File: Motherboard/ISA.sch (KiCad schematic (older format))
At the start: 2 parts, among them J2 Bus_ISA_8bit, J3 Bus_ISA_8bit

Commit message: A VERY large sync...
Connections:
- net GND: now reaches J2.1 (GND)
- net GND: now also J2.10 (GND), J2.31 (GND), J3.1 (GND), J3.10 (GND), J3.31 (GND)
- net +5V: now reaches J2.29 (VCC)
- net +5V: now also J2.3 (VCC), J3.29 (VCC), J3.3 (VCC)
- net -5V: now reaches J2.5 (-5V)
- net -5V: now also J3.5 (-5V)
- net -12V: now reaches J2.7 (-12V)
- net -12V: now also J3.7 (-12V)
- net +12V: now reaches J2.9 (+12V)
- net +12V: now also J3.9 (+12V)
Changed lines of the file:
@@
 $Descr A4 11693 8268
 encoding utf-8
-Sheet 5 5
+Sheet 5 8
 Title ""
 Date ""
@@
 	1    0    0    -1
 $EndComp
+$Comp
+L power:GND #PWR0110
+U 1 1 5C3285DE
+P 2275 1800
+F 0 "#PWR0110" H 2275 1550 50  0001 C CNN
+F 1 "GND" H 2280 1627 50  0000 C CNN
+F 2 "" H 2275 1800 50  0001 C CNN
+F 3 "" H 2275 1800 50  0001 C CNN
+	1    2275 1800
+	-1   0    0    1
+$EndComp
+Wire Wire Line
+	2275 1800 2275 1900
+Wire Wire Line
+	2275 1900 2350 1900
+$Comp
+L power:+5V #PWR0111
+U 1 1 5C3286C5
+P 2050 1800
+F 0 "#PWR0111" H 2050 1650 50  0001 C CNN
+F 1 "+5V" H 2065 1973 50  0000 C CNN
+F 2 "" H 2050 1800 50  0001 C CNN
+F 3 "" H 2050 1800 50  0001 C CNN
+	1    2050 1800
+	1    0    0    -1
+$EndComp
+Wire Wire Line
+	2050 1800 2050 2100
+Wire Wire Line
+	2050 2100 2350 2100
+$Comp
+L power:-5V #PWR0112
+U 1 1 5C3287A9
+P 2050 2300
+F 0 "#PWR0112" H 2050 2400 50  0001 C CNN
+F 1 "-5V" V 2065 2428 50  0000 L CNN
+F 2 "" H 2050 2300 50  0001 C CNN
+F 3 "" H 2050 2300 50  0001 C CNN
+	1    2050 2300
+	0    -1   -1   0
+$EndComp
+Wire Wire Line
+	2050 2300 2350 2300
+Wire Wire Line
+	2350 2500 2050 2500
+Wire Wire Line
+	2350 2700 2050 2700
+Wire Wire Line
+	2350 2800 2050 2800
+$Comp
+L power:-12V #PWR0113
+U 1 1 5C328963
+P 2050 2500
+F 0 "#PWR0113" H 2050 2600 50  0001 C CNN
+F 1 "-12V" V 2065 2628 50  0000 L CNN
+F 2 "" H 2050 2500 50  0001 C CNN
+F 3 "" H 2050 2500 50  0001 C CNN
+	1    2050 2500
+	0    -1   -1   0
+$EndComp
+$Comp
+L power:+12V #PWR0114
+U 1 1 5C3289C0
+P 2050 2700
+F 0 "#PWR0114" H 2050 2550 50  0001 C CNN
+F 1 "+12V" V 2065 2828 50  0000 L CNN
+F 2 "" H 2050 2700 50  0001 C CNN
+F 3 "" H 2050 2700 50  0001 C CNN
+	1    2050 2700
+	0    -1   -1   0
+$EndComp
+$Comp
+L power:GND #PWR0115
+U 1 1 5C328A08
+P 2050 2800
+F 0 "#PWR0115" H 2050 2550 50  0001 C CNN
+F 1 "GND" V 2055 2672 50  0000 R CNN
+F 2 "" H 2050 2800 50  0001 C CNN
+F 3 "" H 2050 2800 50  0001 C CNN
+	1    2050 2800
+	0    1    1    0
+$EndComp
+Wire Wire Line
+	2350 4700 2100 4700
+$Comp
+L power:+5V #PWR0116
+U 1 1 5C328B26
+P 2100 4700
+F 0 "#PWR0116" H 2100 4550 50  0001 C CNN
+F 1 "+5V" V 2115 4828 50  0000 L CNN
+F 2 "" H 2100 4700 50  0001 C CNN
+F 3 "" H 2100 4700 50  0001 C CNN
+	1    2100 4700
+	0    -1   -1   0
+$EndComp
+Wire Wire Line
+	2350 4900 2100 4900
+$Comp
+L power:GND #PWR0117
+U 1 1 5C328BFE
+P 2100 4900
+F 0 "#PWR0117" H 2100 4650 50  0001 C CNN
+F 1 "GND" V 2105 4772 50  0000 R CNN
+F 2 "" H 2100 4900 50  0001 C CNN
+F 3 "" H 2100 4900 50  0001 C CNN
+	1    2100 4900
+	0    1    1    0
+$EndComp
+$Comp
+L power:GND #PWR0118
+U 1 1 5C328D0A
+P 4850 1800
+F 0 "#PWR0118" H 4850 1550 50  0001 C CNN
+F 1 "GND" H 4855 1627 50  0000 C CNN
+F 2 "" H 4850 1800 50  0001 C CNN
+F 3 "" H 4850 1800 50  0001 C CNN
+	1    4850 1800
+	-1   0    0    1
+$EndComp
+Wire Wire Line
+	4850 1800 4850 1900
+Wire Wire Line
+	4850 1900 4925 1900
+$Comp
+L power:+5V #PWR0119
+U 1 1 5C328D12
+P 4625 1800
+F 0 "#PWR0119" H 4625 1650 50  0001 C CNN
+F 1 "+5V" H 4640 1973 50  0000 C CNN
+F 2 "" H 4625 1800 50  0001 C CNN
+F 3 "" H 4625 1800 50  0001 C CNN
+	1    4625 1800
+	1    0    0    -1
+$EndComp
+Wire Wire Line
+	4625 1800 4625 2100
+Wire Wire Line
+	4625 2100 4925 2100
+$Comp
+L power:-5V #PWR0120
+U 1 1 5C328D1A
+P 4625 2300
+F 0 "#PWR0120" H 4625 2400 50  0001 C CNN
+F 1 "-5V" V 4640 2428 50  0000 L CNN
+F 2 "" H 4625 2300 50  0001 C CNN
+F 3 "" H 4625 2300 50  0001 C CNN
+	1    4625 2300
+	0    -1   -1   0
+$EndComp
+Wire Wire Line
+	4625 2300 4925 2300
+Wire Wire Line
+	4925 2500 4625 2500
+Wire Wire Line
+	4925 2700 4625 2700
+Wire Wire Line
+	4925 2800 4625 2800
+$Comp
+L power:-12V #PWR0121
+U 1 1 5C328D24
+P 4625 2500
+F 0 "#PWR0121" H 4625 2600 50  0001 C CNN
+F 1 "-12V" V 4640 2628 50  0000 L CNN
+F 2 "" H 4625 2500 50  0001 C CNN
+F 3 "" H 4625 2500 50  0001 C CNN
+	1    4625 2500
+	0    -1   -1   0
+$EndComp
+$Comp
+L power:+12V #PWR0122
+U 1 1 5C328D2A
+P 4625 2700
+F 0 "#PWR0122" H 4625 2550 50  0001 C CNN
+F 1 "+12V" V 4640 2828 50  0000 L CNN
+F 2 "" H 4625 2700 50  0001 C CNN
+F 3 "" H 4625 2700 50  0001 C CNN
+	1    4625 2700
+	0    -1   -1   0
+$EndComp
+$Comp
+L power:GND #PWR0123
+U 1 1 5C328D30
+P 4625 2800
+F 0 "#PWR0123" H 4625 2550 50  0001 C CNN
+F 1 "GND" V 4630 2672 50  0000 R CNN
+F 2 "" H 4625 2800 50  0001 C CNN
+F 3 "" H 4625 2800 50  0001 C CNN
+	1    4625 2800
+	0    1    1    0
+$EndComp
+Wire Wire Line
+	4925 4700 4675 4700
+$Comp
+L power:+5V #PWR0124
+U 1 1 5C328D37
+P 4675 4700
+F 0 "#PWR0124" H 4675 4550 50  0001 C CNN
+F 1 "+5V" V 4690 4828 50  0000 L CNN
+F 2 "" H 4675 4700 50  0001 C CNN
+F 3 "" H 4675 4700 50  0001 C CNN
+	1    4675 4700
+	0    -1   -1   0
+$EndComp
+Wire Wire Line
+	4925 4900 4675 4900
+$Comp
+L power:GND #PWR0125
+U 1 1 5C328D3E
+P 4675 4900
+F 0 "#PWR0125" H 4675 4650 50  0001 C CNN
+F 1 "GND" V 4680 4772 50  0000 R CNN
+F 2 "" H 4675 4900 50  0001 C CNN
+F 3 "" H 4675 4900 50  0001 C CNN
+	1    4675 4900
+	0    1    1    0
+$EndComp
 $EndSCHEMATC

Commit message: Large sync
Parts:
- added J5, J6: Bus_ISA_8bit, RetPC:ISA-8-bit, symbol Connector:Bus_ISA_8bit
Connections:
- net +12V: now also J5.9 (+12V), J6.9 (+12V)
- net +5V: now also J5.29 (VCC), J5.3 (VCC), J6.29 (VCC), J6.3 (VCC)
- net -12V: now also J5.7 (-12V), J6.7 (-12V)
- net -5V: now also J5.5 (-5V), J6.5 (-5V)
- net GND: now also J5.1 (GND), J5.10 (GND), J5.31 (GND), J6.1 (GND), J6.10 (GND), J6.31 (GND)
- net RESET: now reaches J2.2 (RESET)
- net RESET: now also J3.2 (RESET), J5.2 (RESET), J6.2 (RESET)
- no-connect marks 0 -> 4

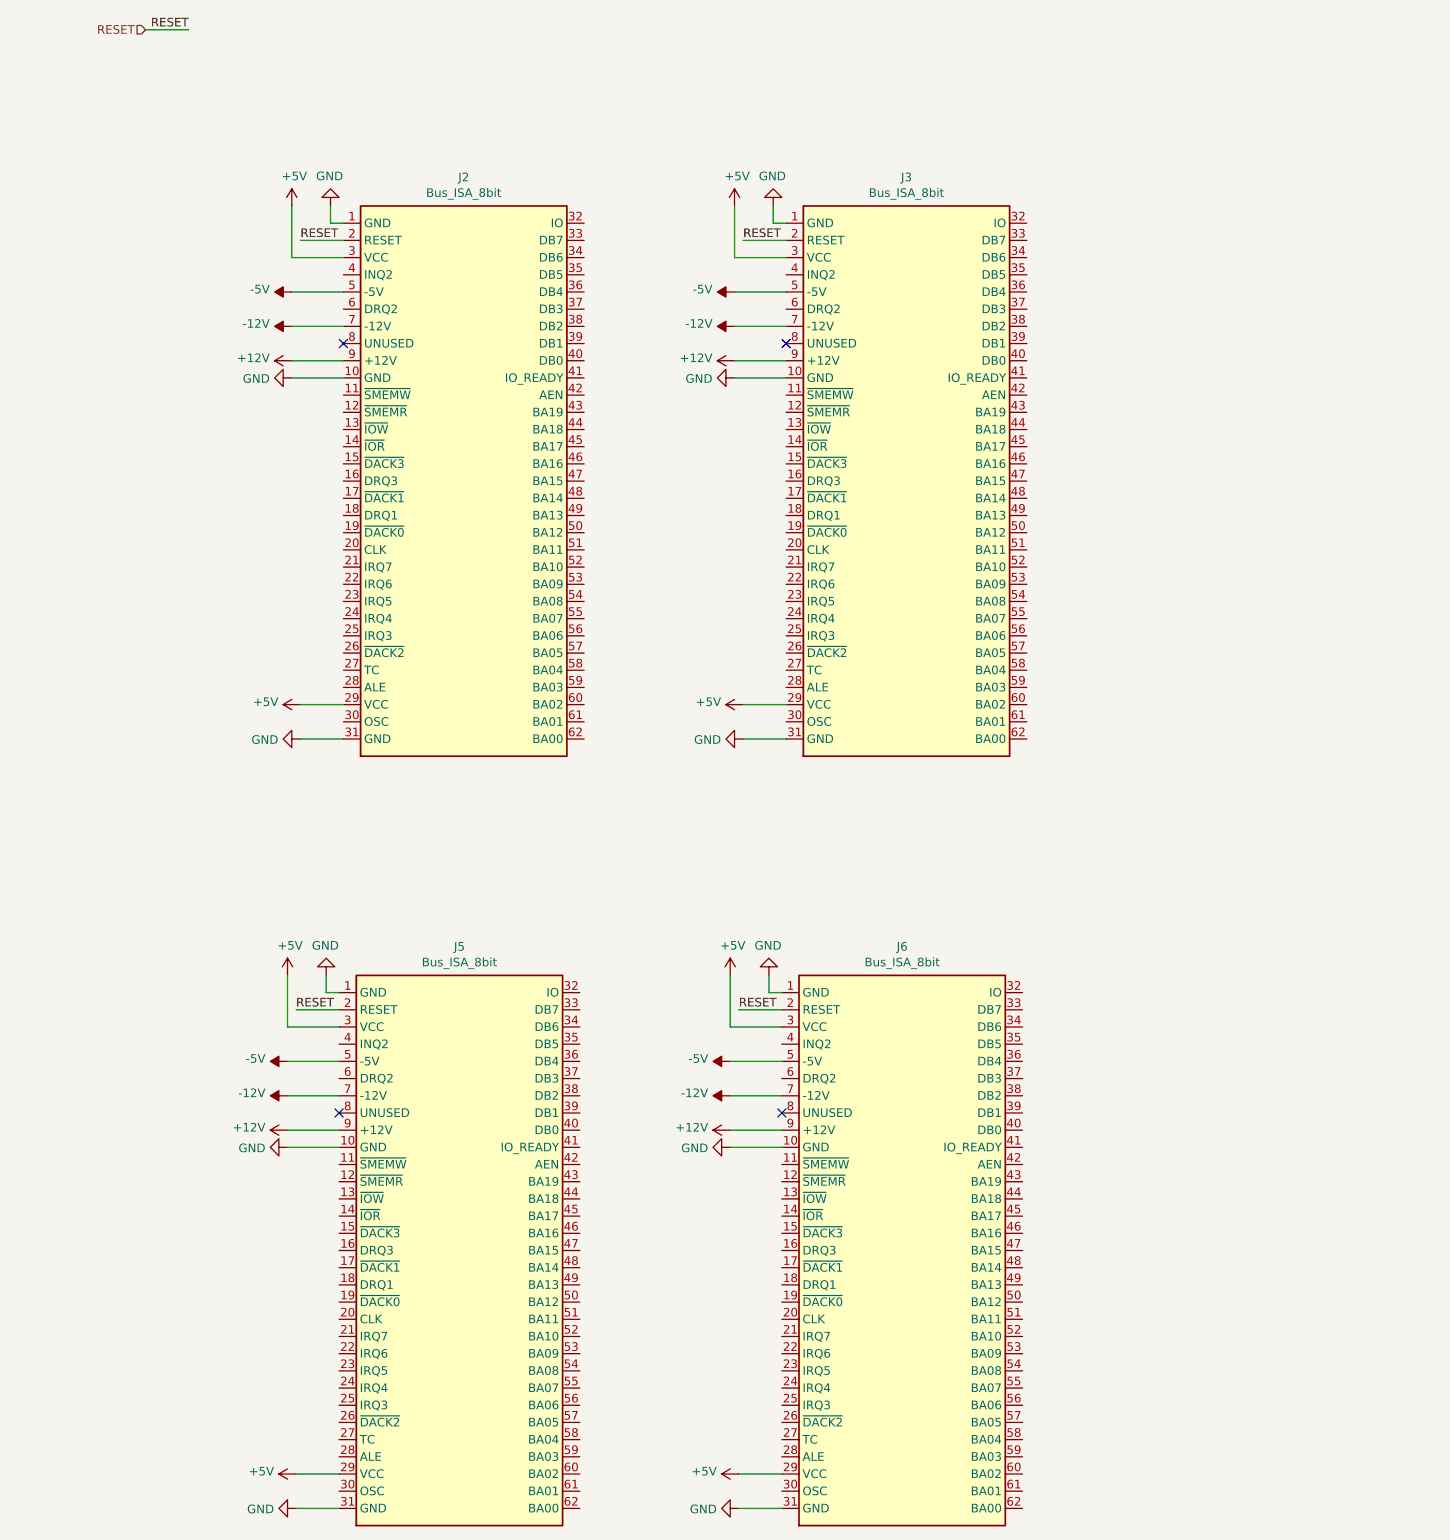
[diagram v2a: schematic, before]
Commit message: Work on motherboard  - Integrating glue logic into CPLD  - Began work on routing
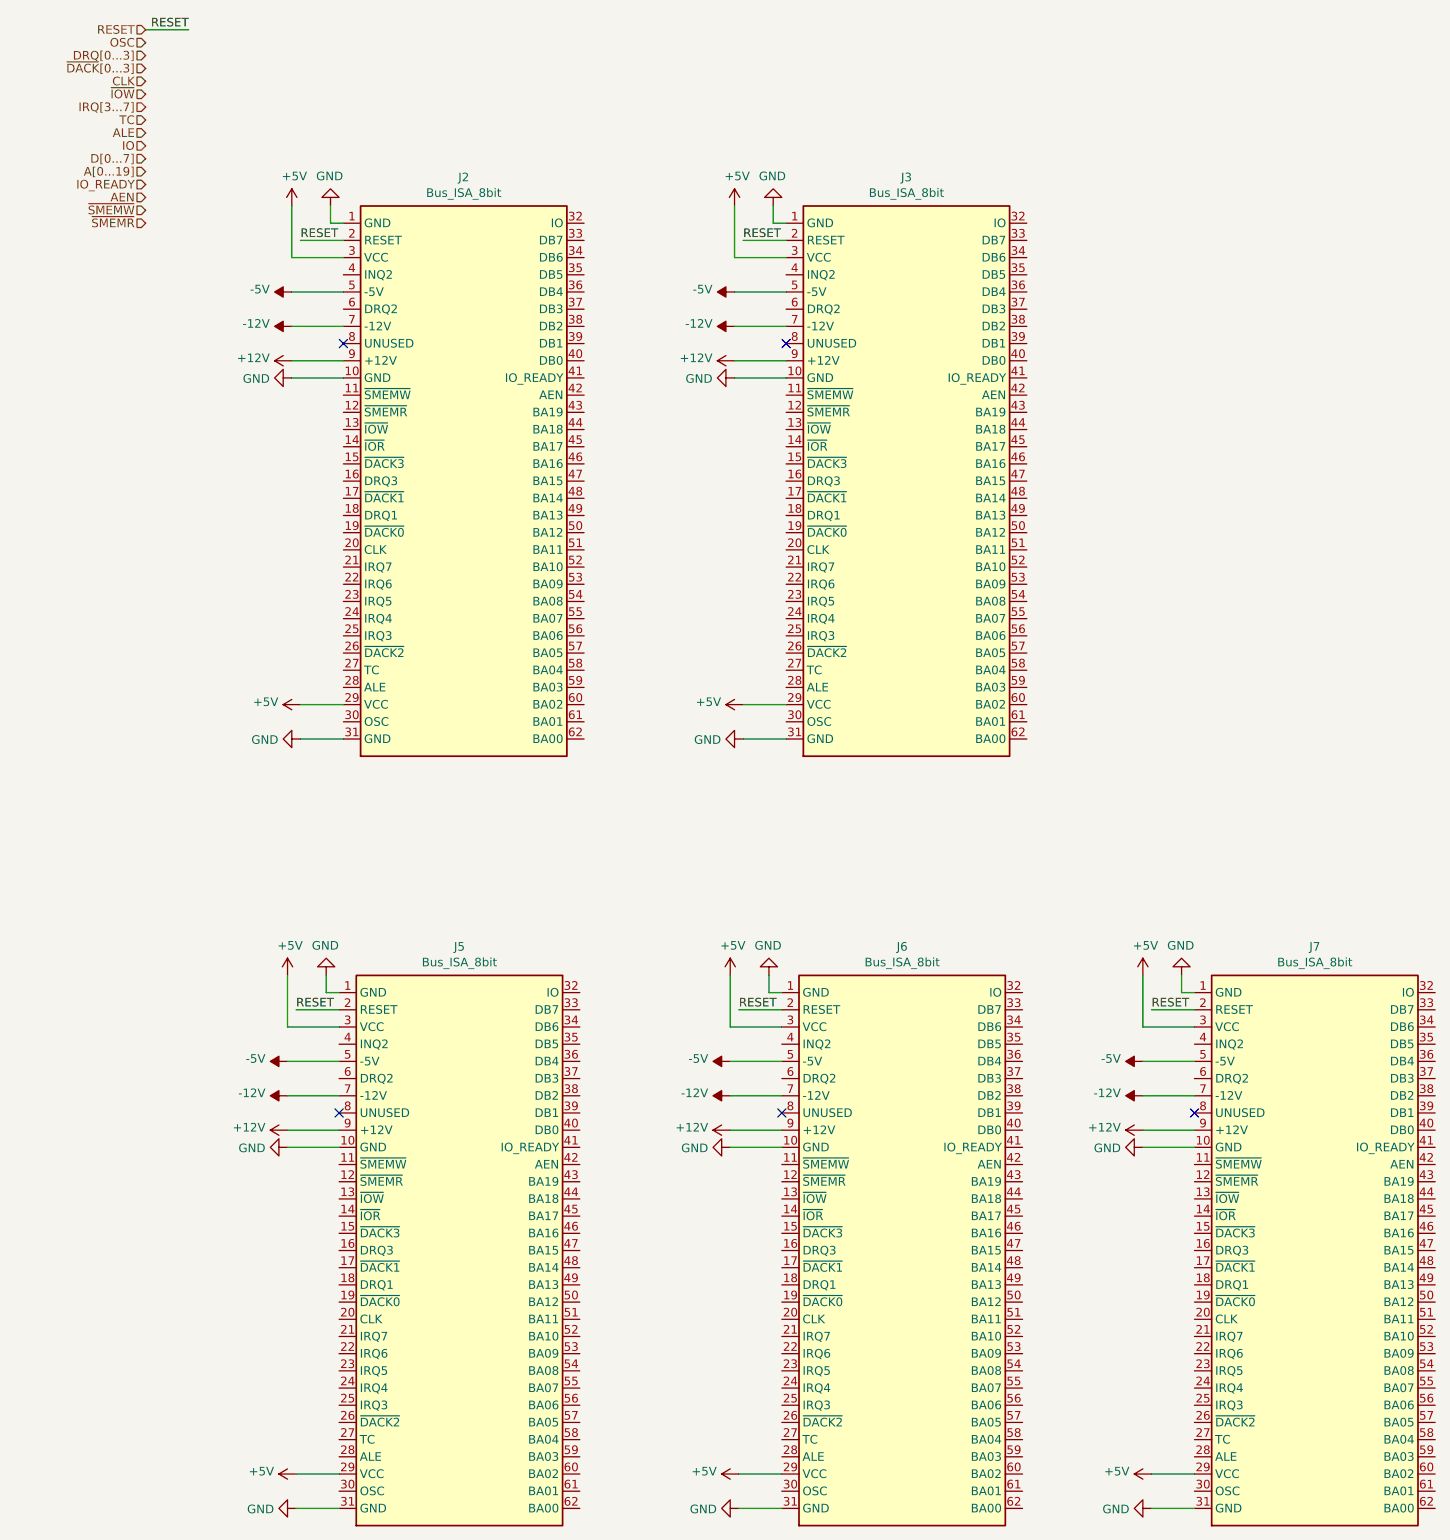
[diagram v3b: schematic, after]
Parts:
- added J7: Bus_ISA_8bit, RetPC:ISA-8-bit, symbol Connector:Bus_ISA_8bit
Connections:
- net +12V: now also J7.9 (+12V)
- net +5V: now also J7.29 (VCC), J7.3 (VCC)
- net -12V: now also J7.7 (-12V)
- net -5V: now also J7.5 (-5V)
- net GND: now also J7.1 (GND), J7.10 (GND), J7.31 (GND)
- net RESET: now also J7.2 (RESET)
- no-connect marks 4 -> 5
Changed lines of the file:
@@
 Text Label 4650 6475 0    50   ~ 0
 RESET
+$Comp
+L Connector:Bus_ISA_8bit J7
+U 1 1 5C5AC837
+P 8000 7875
+F 0 "J7" H 8000 9642 50  0000 C CNN
+F 1 "Bus_ISA_8bit" H 8000 9551 50  0000 C CNN
+F 2 "RetPC:ISA-8-bit" H 8000 7875 50  0001 C CNN
+F 3 "https://en.wikipedia.org/wiki/Industry_Standard_Architecture" H 8000 7875 50  0001 C CNN
+	1    8000 7875
+	1    0    0    -1
+$EndComp
+$Comp
+L power:GND #PWR0148
+U 1 1 5C5AC83D
+P 7225 6275
+F 0 "#PWR0148" H 7225 6025 50  0001 C CNN
+F 1 "GND" H 7230 6102 50  0000 C CNN
+F 2 "" H 7225 6275 50  0001 C CNN
+F 3 "" H 7225 6275 50  0001 C CNN
+	1    7225 6275
+	-1   0    0    1
+$EndComp
+Wire Wire Line
+	7225 6275 7225 6375
+Wire Wire Line
+	7225 6375 7300 6375
+$Comp
+L power:+5V #PWR0149
+U 1 1 5C5AC845
+P 7000 6275
+F 0 "#PWR0149" H 7000 6125 50  0001 C CNN
+F 1 "+5V" H 7015 6448 50  0000 C CNN
+F 2 "" H 7000 6275 50  0001 C CNN
+F 3 "" H 7000 6275 50  0001 C CNN
+	1    7000 6275
+	1    0    0    -1
+$EndComp
+Wire Wire Line
+	7000 6275 7000 6575
+Wire Wire Line
+	7000 6575 7300 6575
+$Comp
+L power:-5V #PWR0150
+U 1 1 5C5AC84D
+P 7000 6775
+F 0 "#PWR0150" H 7000 6875 50  0001 C CNN
+F 1 "-5V" V 7015 6903 50  0000 L CNN
+F 2 "" H 7000 6775 50  0001 C CNN
+F 3 "" H 7000 6775 50  0001 C CNN
+	1    7000 6775
+	0    -1   -1   0
+$EndComp
+Wire Wire Line
+	7000 6775 7300 6775
+Wire Wire Line
+	7300 6975 7000 6975
+Wire Wire Line
+	7300 7175 7000 7175
+Wire Wire Line
+	7300 7275 7000 7275
+$Comp
+L power:-12V #PWR0151
+U 1 1 5C5AC857
+P 7000 6975
+F 0 "#PWR0151" H 7000 7075 50  0001 C CNN
+F 1 "-12V" V 7015 7103 50  0000 L CNN
+F 2 "" H 7000 6975 50  0001 C CNN
+F 3 "" H 7000 6975 50  0001 C CNN
+	1    7000 6975
+	0    -1   -1   0
+$EndComp
+$Comp
+L power:+12V #PWR0152
+U 1 1 5C5AC85D
+P 7000 7175
+F 0 "#PWR0152" H 7000 7025 50  0001 C CNN
+F 1 "+12V" V 7015 7303 50  0000 L CNN
+F 2 "" H 7000 7175 50  0001 C CNN
+F 3 "" H 7000 7175 50  0001 C CNN
+	1    7000 7175
+	0    -1   -1   0
+$EndComp
+$Comp
+L power:GND #PWR0153
+U 1 1 5C5AC863
+P 7000 7275
+F 0 "#PWR0153" H 7000 7025 50  0001 C CNN
+F 1 "GND" V 7005 7147 50  0000 R CNN
+F 2 "" H 7000 7275 50  0001 C CNN
+F 3 "" H 7000 7275 50  0001 C CNN
+	1    7000 7275
+	0    1    1    0
+$EndComp
+Wire Wire Line
+	7300 9175 7050 9175
+$Comp
+L power:+5V #PWR0154
+U 1 1 5C5AC86A
+P 7050 9175
+F 0 "#PWR0154" H 7050 9025 50  0001 C CNN
+F 1 "+5V" V 7065 9303 50  0000 L CNN
+F 2 "" H 7050 9175 50  0001 C CNN
+F 3 "" H 7050 9175 50  0001 C CNN
+	1    7050 9175
+	0    -1   -1   0
+$EndComp
+Wire Wire Line
+	7300 9375 7050 9375
+$Comp
+L power:GND #PWR0155
+U 1 1 5C5AC871
+P 7050 9375
+F 0 "#PWR0155" H 7050 9125 50  0001 C CNN
+F 1 "GND" V 7055 9247 50  0000 R CNN
+F 2 "" H 7050 9375 50  0001 C CNN
+F 3 "" H 7050 9375 50  0001 C CNN
+	1    7050 9375
+	0    1    1    0
+$EndComp
+NoConn ~ 7300 7075
+Wire Wire Line
+	7300 6475 7050 6475
+Text Label 7050 6475 0    50   ~ 0
+RESET
+Text HLabel 1200 850  0    50   Input ~ 0
+OSC
+Text HLabel 1200 925  0    50   Input ~ 0
+DRQ[0...3]
+Text HLabel 1200 1000 0    50   Input ~ 0
+~DACK~[0...3]
+Text HLabel 1200 1075 0    50   Input ~ 0
+CLK
+Text HLabel 1200 1150 0    50   Input ~ 0
+~IOW
+Text HLabel 1200 1225 0    50   Input ~ 0
+IRQ[3...7]
+Text HLabel 1200 1300 0    50   Input ~ 0
+TC
+Text HLabel 1200 1375 0    50   Input ~ 0
+ALE
+Text HLabel 1200 1450 0    50   Input ~ 0
+IO
+Text HLabel 1200 1525 0    50   Input ~ 0
+D[0...7]
+Text HLabel 1200 1600 0    50   Input ~ 0
+A[0...19]
+Text HLabel 1200 1675 0    50   Input ~ 0
+IO_READY
+Text HLabel 1200 1750 0    50   Input ~ 0
+AEN
+Text HLabel 1200 1825 0    50   Input ~ 0
+~SMEMW
+Text HLabel 1200 1900 0    50   Input ~ 0
+~SMEMR
 $EndSCHEMATC

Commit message: from pc sync
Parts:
- J2, J3, J5, J6, J7: symbol Connector:Bus_ISA_8bit -> Motherboard-rescue:Bus_ISA_8bit-Connector
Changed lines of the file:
@@
 $EndDescr
 $Comp
-L Connector:Bus_ISA_8bit J2
+L Motherboard-rescue:Bus_ISA_8bit-Connector J2
 U 1 1 5C18FAE4
 P 3050 3400
@@
 $EndComp
 $Comp
-L Connector:Bus_ISA_8bit J3
+L Motherboard-rescue:Bus_ISA_8bit-Connector J3
 U 1 1 5C18FB45
 P 5625 3400
@@
 RESET
 $Comp
-L Connector:Bus_ISA_8bit J5
+L Motherboard-rescue:Bus_ISA_8bit-Connector J5
 U 1 1 5C4AF46C
 P 3025 7875
@@
 $EndComp
 $Comp
-L Connector:Bus_ISA_8bit J6
+L Motherboard-rescue:Bus_ISA_8bit-Connector J6
 U 1 1 5C4AF472
 P 5600 7875
@@
 RESET
 $Comp
-L Connector:Bus_ISA_8bit J7
+L Motherboard-rescue:Bus_ISA_8bit-Connector J7
 U 1 1 5C5AC837
 P 8000 7875
